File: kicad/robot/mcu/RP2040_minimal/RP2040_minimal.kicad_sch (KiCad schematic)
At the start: 36 parts, among them J2 Conn_02x07_Counter_Clockwise, Q5 SN74AHC125RGYR, U2 W25Q128JVS, U3 RP2040, Y1 ECS-120-8-36-CKM-TR3

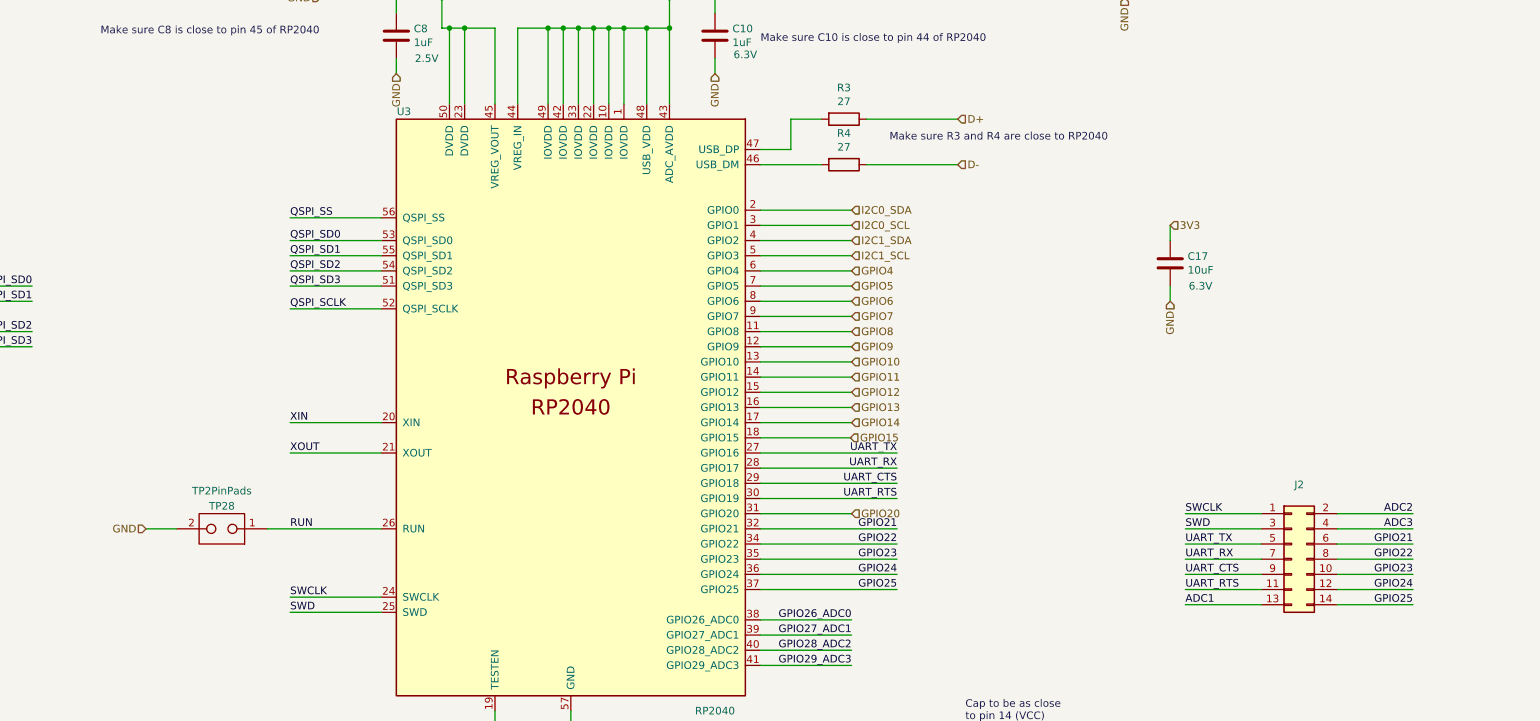
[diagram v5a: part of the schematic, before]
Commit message: Adding a few options for pin headers for GPIO unused and UART
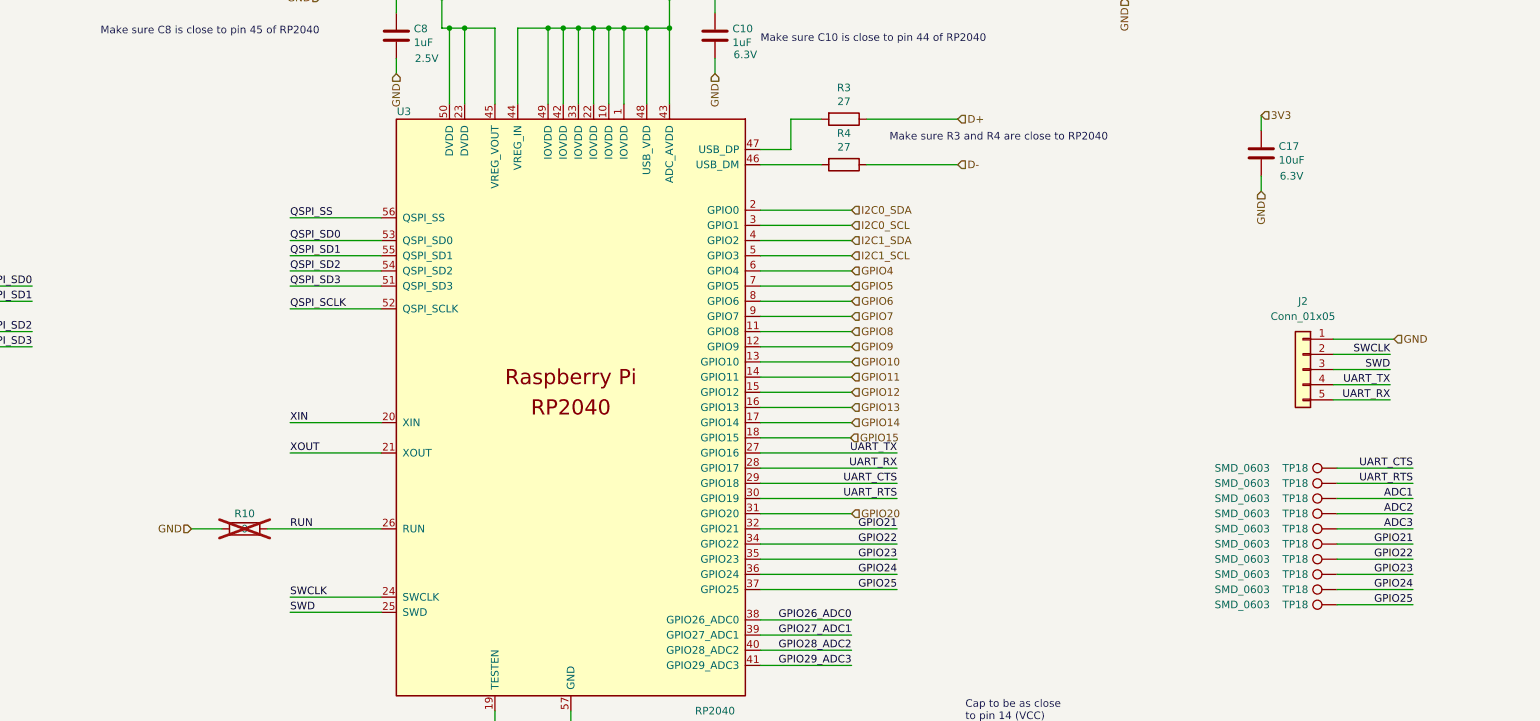
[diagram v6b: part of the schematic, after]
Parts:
- removed J2: Conn_02x07_Counter_Clockwise, robot:PinHeader_2x07_P2.54mm_Vertical, symbol robot:Conn_02x07_Odd_Even
- removed TP28: TP2PinPads, robot:TestPoint_2Pads_Pitch2mm_SMD, symbol robot:TestPoint_CurrentShunt
- added J2: Conn_01x05, robot:PinSocket_1x05_P1.00mm_Vertical, symbol Connector_Generic:Conn_01x05
- added R10: 0, robot:R_0603_1608Metric, symbol Device:R
- added TP18 (x10): SMD_0603, robot:TestPoint_SMD_0603, symbol robot:TestPoint
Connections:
- net ADC1: now also TP18.1
- net ADC2: now also TP18.1
- net ADC3: now also TP18.1
- net GND: now also J2.1 (Pin_1), R10.1
- net GPIO21: now also TP18.1
- net GPIO22: now also TP18.1
- net GPIO23: now also TP18.1
- net GPIO24: now also TP18.1
- net GPIO25: now also TP18.1
- net RUN: now also R10.2
- net SWCLK: now also J2.2 (Pin_2)
- net SWD: now also J2.3 (Pin_3)
- net UART_CTS: now also TP18.1
- net UART_RTS: now also TP18.1
- net UART_RX: now also J2.5 (Pin_5)
- net UART_TX: now also J2.4 (Pin_4)
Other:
- moved on the sheet: C17

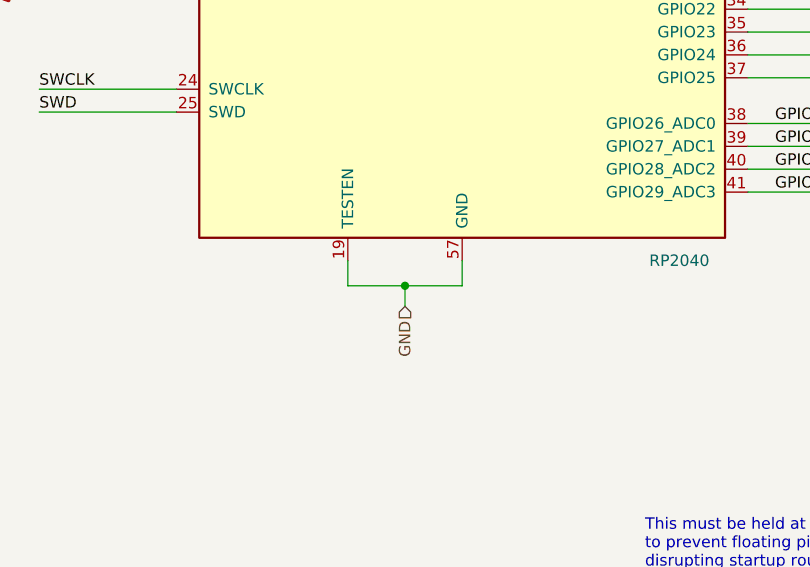
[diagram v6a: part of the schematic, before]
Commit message: Realigning things to grid
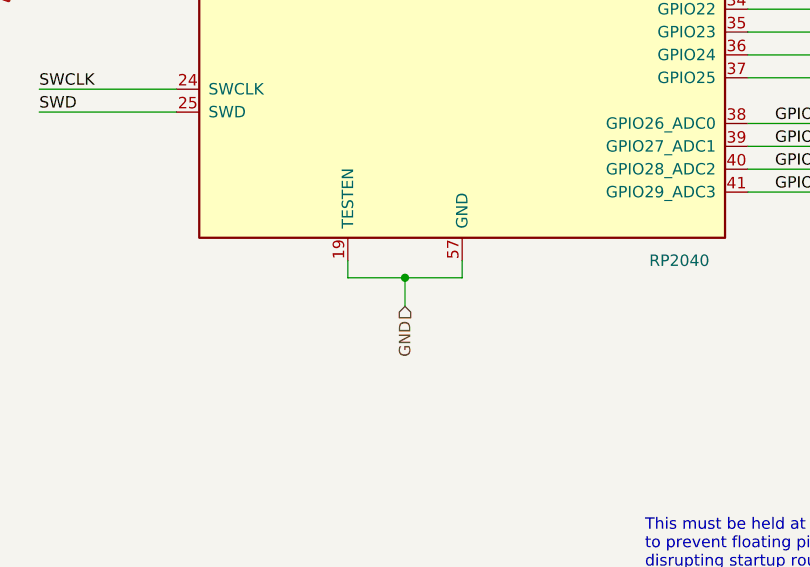
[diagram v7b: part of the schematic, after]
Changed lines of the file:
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@@
   (junction (at 45.72 224.79) (diameter 0) (color 0 0 0 0)
   )
-  (junction (at 193.04 198.374) (diameter 0) (color 0 0 0 0)
-  )
   (junction (at 200.66 81.28) (diameter 0) (color 0 0 0 0)
   )
@@
   (junction (at 269.24 73.66) (diameter 0) (color 0 0 0 0)
   )
+  (junction (at 193.04 197.485) (diameter 0) (color 0 0 0 0)
+  )
   (junction (at 66.04 228.6) (diameter 0) (color 0 0 0 0)
   )
@@
     (stroke (width 0) (type default))
   )
-  (wire (pts (xy 186.69 195.58) (xy 186.69 198.374))
+  (wire (pts (xy 186.69 195.58) (xy 186.69 197.485))
     (stroke (width 0) (type default))
   )
@@
     (stroke (width 0) (type default))
   )
-  (wire (pts (xy 199.39 198.374) (xy 193.04 198.374))
+  (wire (pts (xy 199.39 197.485) (xy 193.04 197.485))
     (stroke (width 0) (type default))
   )
@@
     (stroke (width 0) (type default))
   )
-  (wire (pts (xy 193.04 198.374) (xy 193.04 200.66))
-    (stroke (width 0) (type default))
-  )
   (wire (pts (xy 205.74 81.28) (xy 208.28 81.28))
     (stroke (width 0) (type default))
@@
     (stroke (width 0) (type default))
   )
+  (wire (pts (xy 193.04 197.485) (xy 193.04 200.66))
+    (stroke (width 0) (type default))
+  )
   (wire (pts (xy 231.14 101.6) (xy 236.22 101.6))
     (stroke (width 0) (type default))
@@
     (stroke (width 0) (type default))
   )
-  (wire (pts (xy 186.69 198.374) (xy 193.04 198.374))
+  (wire (pts (xy 186.69 197.485) (xy 193.04 197.485))
     (stroke (width 0) (type default))
   )
@@
     (stroke (width 0) (type default))
   )
-  (wire (pts (xy 199.39 195.58) (xy 199.39 198.374))
-    (stroke (width 0) (type default))
-  )
+  (wire (pts (xy 199.39 195.58) (xy 199.39 197.485))
+    (stroke (width 0) (type default))
+  )

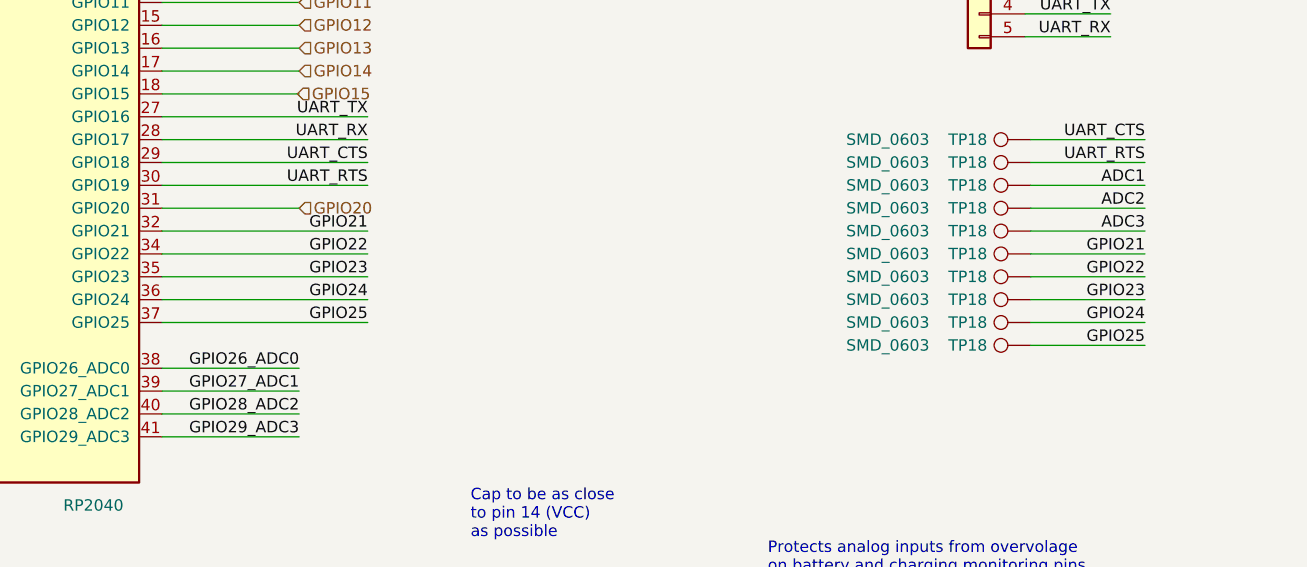
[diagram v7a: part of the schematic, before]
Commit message: Replacing LEDs with side mounted ones, and added an LED driver for the two that don't have a driver
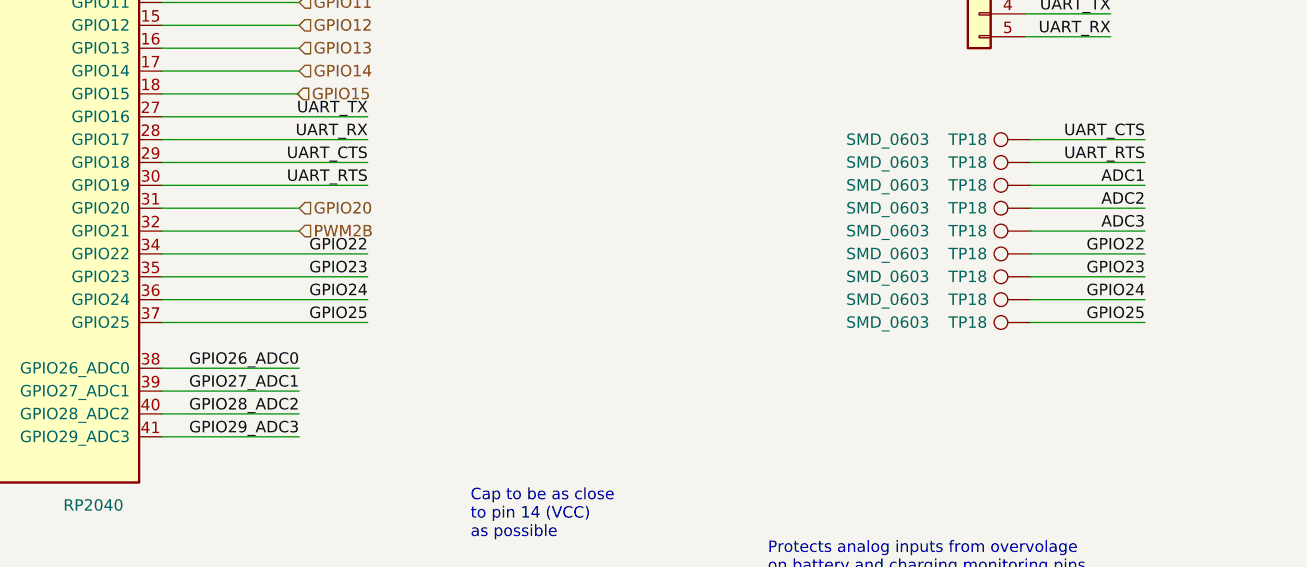
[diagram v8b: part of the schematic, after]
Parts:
- removed TP18: SMD_0603, robot:TestPoint_SMD_0603, symbol robot:TestPoint
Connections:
- net GPIO21: no longer U3.32 (GPIO21)
- new net PWM2B: U3.32 (GPIO21)
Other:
- moved on the sheet: TP18
